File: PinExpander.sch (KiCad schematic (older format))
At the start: 35 parts, among them J1 CONN_01X08, J2 CONN_01X08, J3 CONN_01X08, J4 CONN_01X05, U1 74HC595, U2 74HC595, U3 74HC595

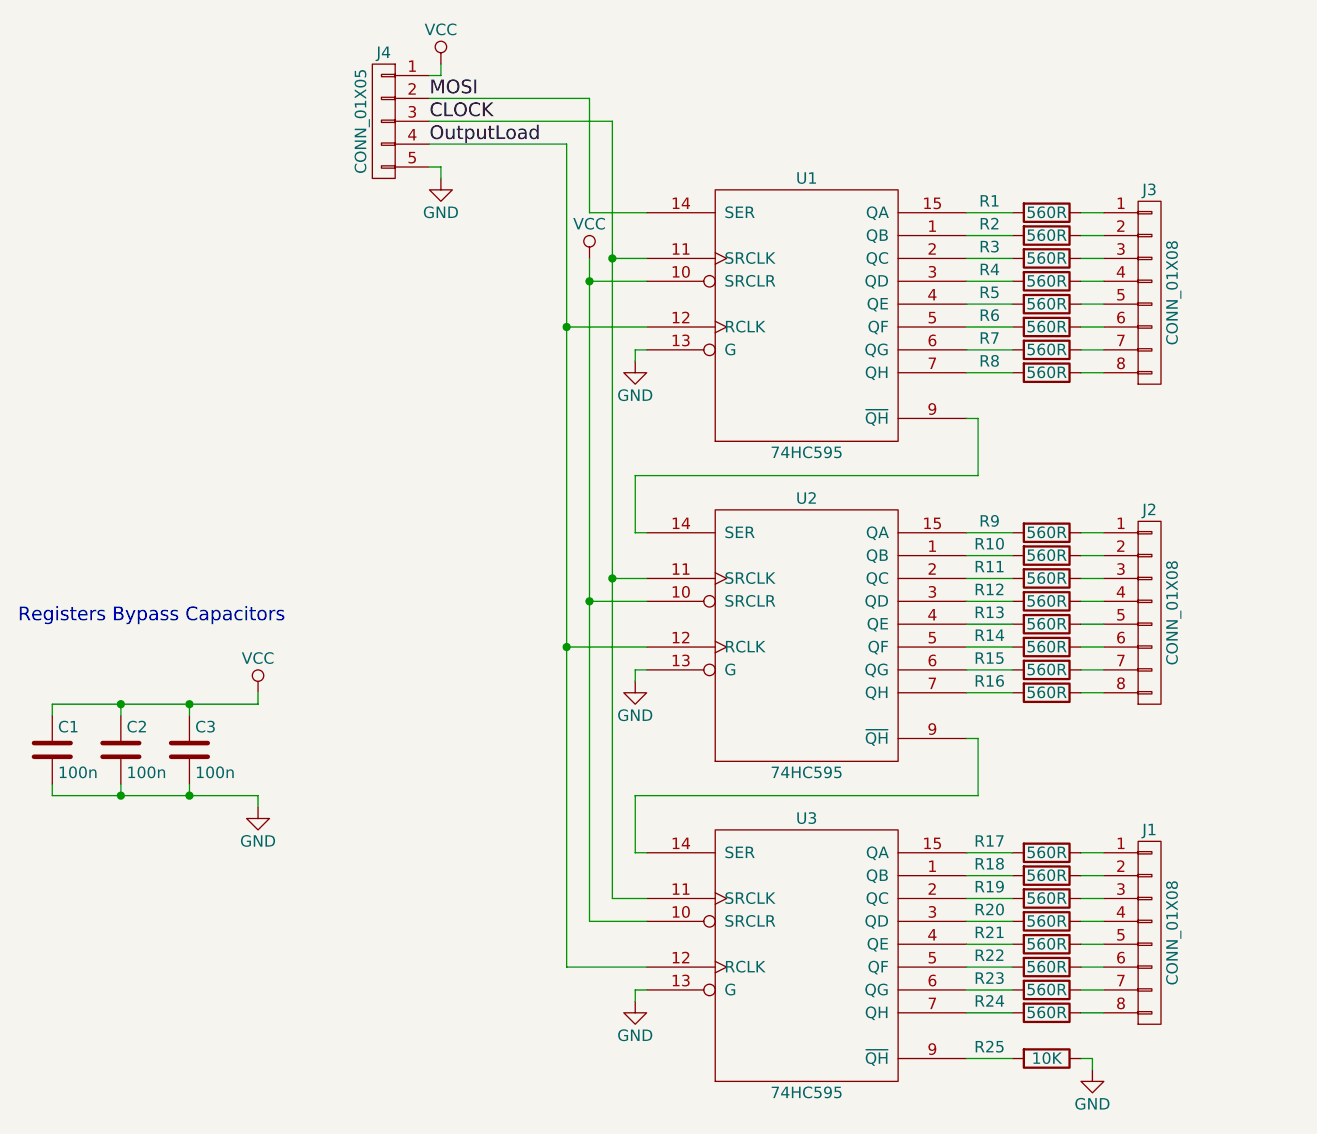
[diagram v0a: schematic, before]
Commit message: New stackable version
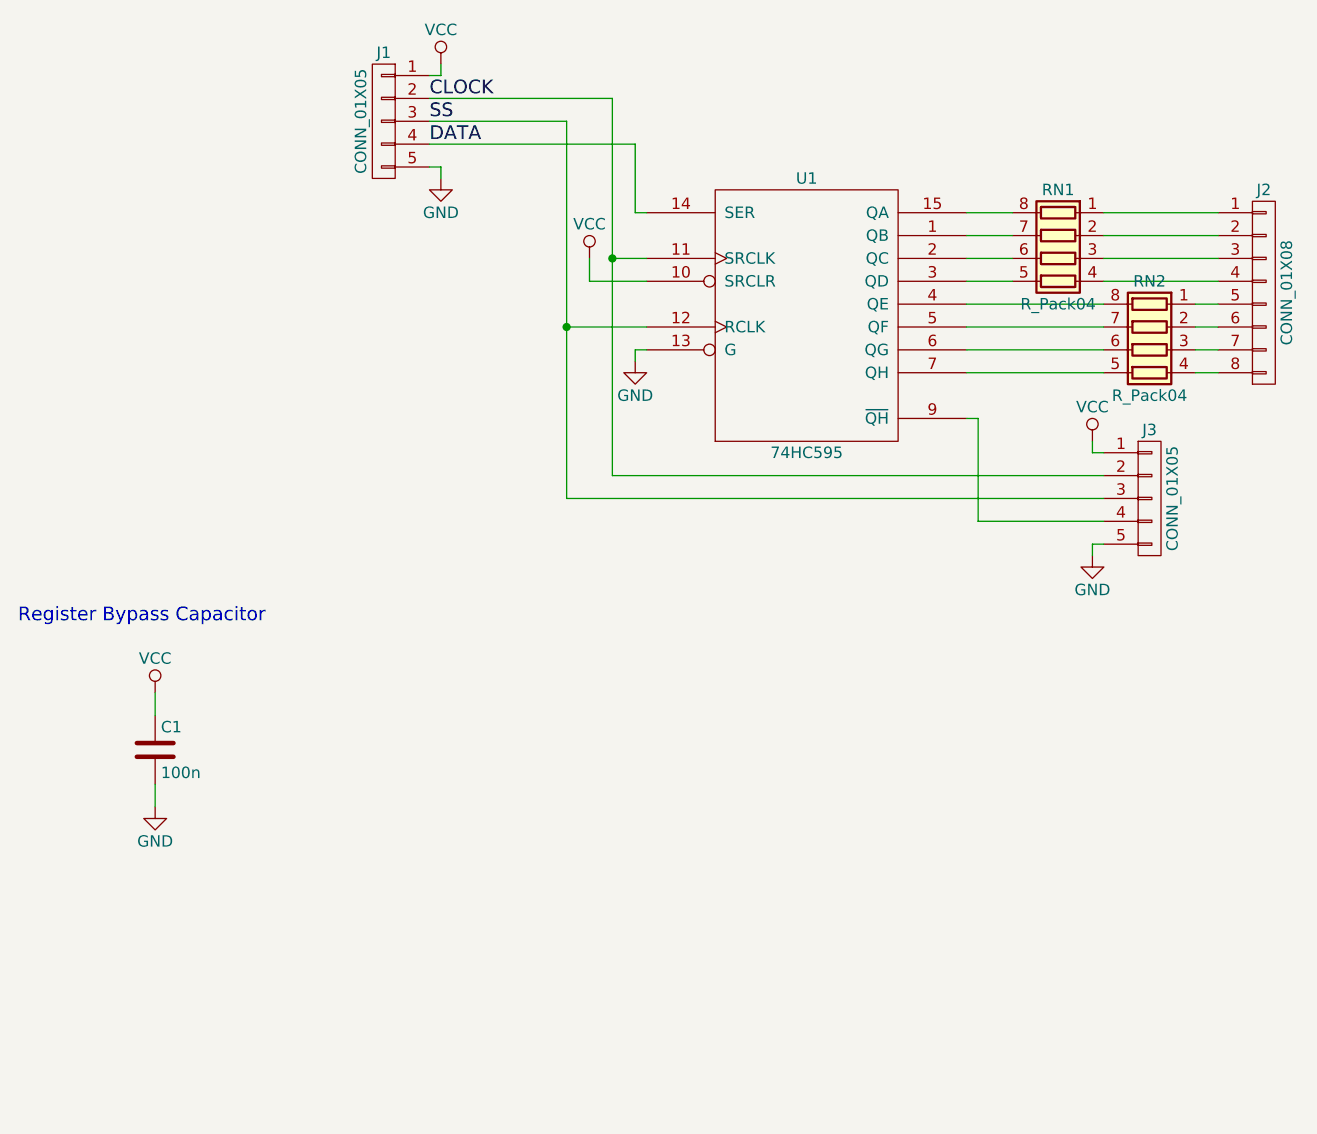
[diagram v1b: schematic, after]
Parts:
- removed C2, C3: 100n, Capacitors_SMD:C_1206_HandSoldering, symbol C
- removed J1, J2: CONN_01X08, Pin_Headers:Pin_Header_Straight_1x08_Pitch2.54mm, symbol CONN_01X08
- removed R1, R10, R11, R12, R13, R14, R15, R16, R17, R18, R19, R2, R20, R21, R22, R23, R24, R3, R4, R5, R6, R7, R8, R9: 560R, Resistors_SMD:R_1206_HandSoldering, symbol R
- removed R25: 10K, Resistors_SMD:R_1206_HandSoldering, symbol R
- removed U2, U3: 74HC595, Housings_SOIC:SOIC-16_3.9x9.9mm_Pitch1.27mm, symbol 74HC595
- added J3: CONN_01X05, Pin_Headers:Pin_Header_Straight_1x05_Pitch2.54mm, symbol CONN_01X05
- added RN1, RN2: R_Pack04, Resistors_SMD:R_Array_Convex_4x0603, symbol R_Pack04
- renumbered J4 to J1, J3 to J2
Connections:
- net CLOCK: now also J1.2 (P2), J3.2 (P2); no longer J1.3 (P3)
- net GND: now also J3.5 (P5)
- net VCC: now also J3.1 (P1)
- net at U1.1 (QB): now also RN1.7 (R2.2)
- net at U1.15 (QA): now also RN1.8 (R1.2)
- net at U1.2 (QC): now also RN1.6 (R3.2)
- net at U1.3 (QD): now also RN1.5 (R4.2)
- net at U1.4 (QE): now also RN2.8 (R1.2)
- net at U1.5 (QF): now also RN2.7 (R2.2)
- net at U1.6 (QG): now also RN2.6 (R3.2)
- net at U1.7 (QH): now also RN2.5 (R4.2)
- net at U1.9 (~QH): now also J3.4 (P4)
- net at J2.1 (P1): now also RN1.1 (R1.1)
- net at J2.2 (P2): now also RN1.2 (R2.1)
- net at J2.3 (P3): now also RN1.3 (R3.1)
- net at J2.4 (P4): now also RN1.4 (R4.1)
- net at J2.5 (P5): now also RN2.1 (R1.1)
- net at J2.6 (P6): now also RN2.2 (R2.1)
- net at J2.7 (P7): now also RN2.3 (R3.1)
- net at J2.8 (P8): now also RN2.4 (R4.1)
- net MOSI renamed DATA
- net DATA: now also J1.4 (P4); no longer J1.2 (P2)
- net OutputLoad renamed SS
- net SS: now also J1.3 (P3), J3.3 (P3); no longer J1.4 (P4)
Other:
- note added: "Register Bypass Capacitor"
- note removed: "Registers Bypass Capacitors"
- moved on the sheet: C1, J2
